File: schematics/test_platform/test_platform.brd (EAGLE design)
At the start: 100 x 65 mm, 13 parts

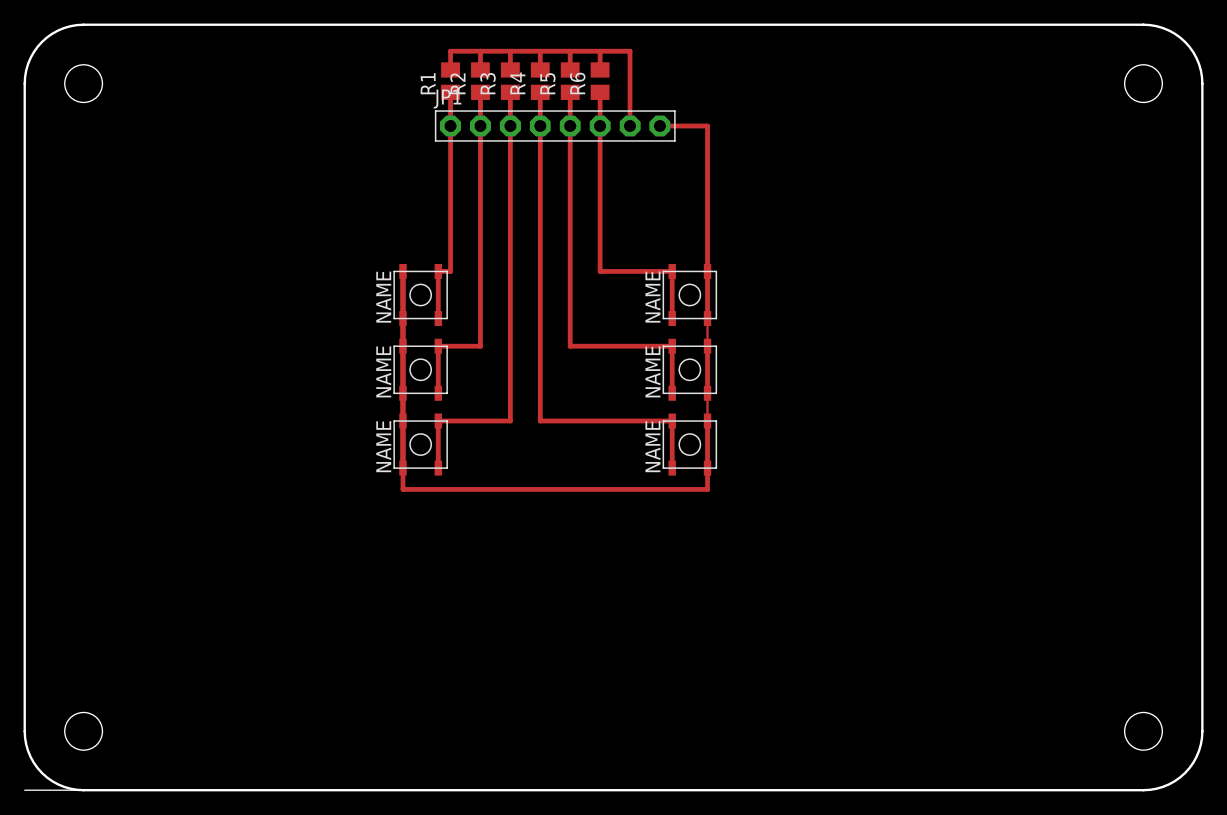
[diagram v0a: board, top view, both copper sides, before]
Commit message: test platform ready for production, except for button footprints
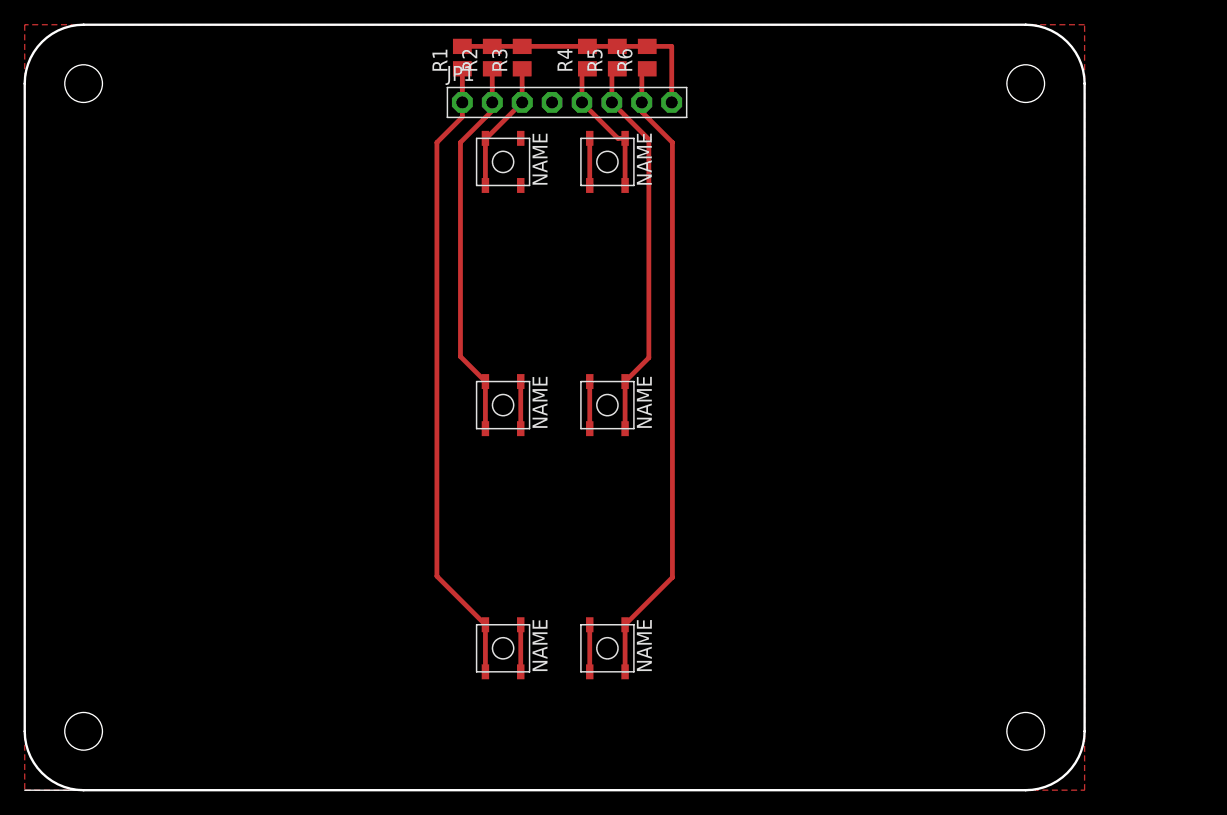
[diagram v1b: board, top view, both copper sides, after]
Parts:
- moved U$1 30.8 mm to (40.6, 12.1), turned to 180 degrees
- moved U$4 30.8 mm to (49.5, 12.1), turned to 180 degrees
- moved U$3 25.0 mm to (40.6, 53.4), turned to 180 degrees
- moved U$6 25.0 mm to (49.5, 53.4), turned to 180 degrees
- moved U$2 7.62 mm to (40.6, 32.7), turned to 180 degrees
- moved U$5 7.62 mm to (49.5, 32.7), turned to 180 degrees
- moved R4 4.47 mm to (47.8, 62.2)
- moved R5 4.47 mm to (50.3, 62.2)
- moved R6 4.47 mm to (52.9, 62.2)
- moved JP1 2.24 mm to (46.0, 58.4)
- moved R1 2.24 mm to (37.2, 62.2)
- moved R2 2.24 mm to (39.7, 62.2)
- moved R3 2.24 mm to (42.2, 62.2)
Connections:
- removed net N$7: JP1.7, R1.2, R2.2, R3.2, R4.2, R5.2, R6.2
- removed net N$8: JP1.8, U$1.A1, U$1.A2, U$2.A1, U$2.A2, U$3.A1, U$3.A2, U$4.B1, U$4.B2, U$5.B1, U$5.B2, U$6.B1, U$6.B2
- new net GND: JP1.4, U$1.A1, U$1.A2, U$2.A1, U$2.A2, U$3.A1, U$3.A2, U$4.B1, U$4.B2, U$5.B1, U$5.B2, U$6.B1, U$6.B2
- new net VCC: JP1.8, R1.2, R2.2, R3.2, R4.2, R5.2, R6.2
- net N$4: now also JP1.5; no longer JP1.4
- net N$5: now also JP1.6; no longer JP1.5
- net N$6: now also JP1.7; no longer JP1.6
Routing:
- net N$8: track 96.0 -> 0.00 mm
- net N$1: track 20.2 -> 53.8 mm
- net N$7: track 31.1 -> 0.00 mm
- net N$4: track 43.1 -> 12.2 mm
- net N$6: track 25.3 -> 54.4 mm
- net N$3: track 38.0 -> 11.2 mm
- net VCC: track 0.00 -> 23.0 mm
- net GND: track 0.00 -> 20.0 mm
- net N$2: track 29.1 -> 32.6 mm
- net N$5: track 34.2 -> 33.2 mm
- added copper zone on layer 1, net GND
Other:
- board size 100 x 65 mm -> 90 x 65 mm

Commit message: circuit for testplatform done
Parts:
- moved U$6 41.4 mm to (50.0, 12.0)
- moved U$4 40.0 mm to (50.0, 52.0), turned to 0 degrees
- moved U$3 1.49 mm to (40.0, 52.0), turned to 0 degrees
- moved U$2 0.94 mm to (40.0, 32.0)
- moved U$5 0.87 mm to (50.0, 32.0)
- moved U$1 0.62 mm to (40.0, 12.0)
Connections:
- net N$4: now also U$4.A1, U$4.A2; no longer U$6.A1, U$6.A2
- net N$6: now also U$6.A1, U$6.A2; no longer U$4.A1, U$4.A2
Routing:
- net GND: track 20.0 -> 0.00 mm
- net N$3: track 11.2 -> 13.3 mm
- net N$1: track 53.8 -> 55.8 mm
- net N$6: track 54.4 -> 56.1 mm
- net N$4: track 12.2 -> 13.8 mm
- net N$5: track 33.2 -> 34.6 mm
- net N$2: track 32.6 -> 34.0 mm
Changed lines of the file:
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@@
 <elements>
 <element name="JP1" library="adafruit" package="1X08-BIG" value="" x="46.05" y="58.4"/>
-<element name="U$1" library="BraillePad" package="SMT-BUTTON" value="SMT_BUTTON" x="40.62" y="12.05" rot="R180"/>
-<element name="U$2" library="BraillePad" package="SMT-BUTTON" value="SMT_BUTTON" x="40.62" y="32.7" rot="R180"/>
-<element name="U$3" library="BraillePad" package="SMT-BUTTON" value="SMT_BUTTON" x="40.62" y="53.35" rot="R180"/>
-<element name="U$4" library="BraillePad" package="SMT-BUTTON" value="SMT_BUTTON" x="49.48" y="12.05" rot="R180"/>
-<element name="U$5" library="BraillePad" package="SMT-BUTTON" value="SMT_BUTTON" x="49.48" y="32.7" rot="R180"/>
-<element name="U$6" library="BraillePad" package="SMT-BUTTON" value="SMT_BUTTON" x="49.48" y="53.35" rot="R180"/>
 <element name="R1" library="rcl" package="M0805" value="" x="37.16" y="62.21" rot="R90"/>
 <element name="R2" library="rcl" package="M0805" value="" x="39.7" y="62.21" rot="R90"/>
@@
 <element name="R6" library="rcl" package="M0805" value="" x="52.86" y="62.21" rot="R90"/>
 <element name="R5" library="rcl" package="M0805" value="" x="50.32" y="62.21" rot="R90"/>
+<element name="U$1" library="BraillePad" package="SMT-BUTTON" value="SMT_BUTTON" x="40" y="12" rot="R180"/>
+<element name="U$2" library="BraillePad" package="SMT-BUTTON" value="SMT_BUTTON" x="40" y="32" rot="R180"/>
+<element name="U$3" library="BraillePad" package="SMT-BUTTON" value="SMT_BUTTON" x="40" y="52"/>
+<element name="U$4" library="BraillePad" package="SMT-BUTTON" value="SMT_BUTTON" x="50" y="52"/>
+<element name="U$5" library="BraillePad" package="SMT-BUTTON" value="SMT_BUTTON" x="50" y="32" rot="R180"/>
+<element name="U$6" library="BraillePad" package="SMT-BUTTON" value="SMT_BUTTON" x="50" y="12" rot="R180"/>
 </elements>
 <signals>
 <signal name="N$1">
 <contactref element="JP1" pad="1"/>
+<contactref element="R1" pad="1"/>
+<wire x1="37.16" y1="58.4" x2="37.16" y2="61.26" width="0.4064" layer="1"/>
 <contactref element="U$1" pad="B1"/>
 <contactref element="U$1" pad="B2"/>
-<contactref element="R1" pad="1"/>
-<wire x1="37.16" y1="58.4" x2="37.16" y2="61.26" width="0.4064" layer="1"/>
-<wire x1="39.12" y1="14.05" x2="39.12" y2="10.05" width="0.4064" layer="1"/>
-<wire x1="37.16" y1="58.4" x2="37.16" y2="57.16" width="0.4064" layer="1"/>
-<wire x1="37.16" y1="57.16" x2="35" y2="55" width="0.4064" layer="1"/>
-<wire x1="35" y1="55" x2="35" y2="18.17" width="0.4064" layer="1"/>
-<wire x1="35" y1="18.17" x2="39.12" y2="14.05" width="0.4064" layer="1"/>
+<wire x1="37.16" y1="58.4" x2="36.4" y2="58.4" width="0.4064" layer="1"/>
+<wire x1="36.4" y1="58.4" x2="35" y2="57" width="0.4064" layer="1"/>
+<wire x1="35" y1="57" x2="35" y2="18.9" width="0.4064" layer="1"/>
+<wire x1="35" y1="18.9" x2="37.9" y2="16" width="0.4064" layer="1"/>
+<wire x1="37.9" y1="16" x2="37.9" y2="8" width="0.4064" layer="1"/>
 </signal>
 <signal name="N$2">
 <contactref element="JP1" pad="2"/>
+<contactref element="R2" pad="1"/>
+<wire x1="39.7" y1="58.4" x2="39.7" y2="61.26" width="0.4064" layer="1"/>
 <contactref element="U$2" pad="B1"/>
 <contactref element="U$2" pad="B2"/>
-<contactref element="R2" pad="1"/>
-<wire x1="39.7" y1="58.4" x2="39.7" y2="61.26" width="0.4064" layer="1"/>
-<wire x1="39.12" y1="34.7" x2="39.12" y2="30.7" width="0.4064" layer="1"/>
-<wire x1="39.7" y1="58.4" x2="39.7" y2="57.7" width="0.4064" layer="1"/>
-<wire x1="39.7" y1="57.7" x2="37" y2="55" width="0.4064" layer="1"/>
-<wire x1="37" y1="55" x2="37" y2="36.82" width="0.4064" layer="1"/>
-<wire x1="37" y1="36.82" x2="39.12" y2="34.7" width="0.4064" layer="1"/>
+<wire x1="39.7" y1="58.4" x2="39.7" y2="37.8" width="0.4064" layer="1"/>
+<wire x1="39.7" y1="37.8" x2="37.9" y2="36" width="0.4064" layer="1"/>
+<wire x1="37.9" y1="28" x2="37.9" y2="36" width="0.4064" layer="1"/>
 </signal>
 <signal name="N$3">
 <contactref element="JP1" pad="3"/>
+<contactref element="R3" pad="1"/>
+<wire x1="42.24" y1="58.4" x2="42.24" y2="61.26" width="0.4064" layer="1"/>
 <contactref element="U$3" pad="B1"/>
 <contactref element="U$3" pad="B2"/>
-<contactref element="R3" pad="1"/>
-<wire x1="42.24" y1="58.4" x2="42.24" y2="61.26" width="0.4064" layer="1"/>
-<wire x1="39.12" y1="55.35" x2="39.12" y2="51.35" width="0.4064" layer="1"/>
-<wire x1="42.24" y1="58.4" x2="39.19" y2="55.35" width="0.4064" layer="1"/>
-<wire x1="39.19" y1="55.35" x2="39.12" y2="55.35" width="0.4064" layer="1"/>
+<wire x1="42.24" y1="58.4" x2="42.1" y2="56" width="0.4064" layer="1"/>
+<wire x1="42.1" y1="48" x2="42.1" y2="56" width="0.4064" layer="1"/>
 </signal>
 <signal name="N$4">
-<contactref element="U$6" pad="A1"/>
-<contactref element="U$6" pad="A2"/>
 <contactref element="R4" pad="1"/>
-<wire x1="50.98" y1="55.35" x2="50.98" y2="51.35" width="0.4064" layer="1"/>
 <contactref element="JP1" pad="5"/>
 <wire x1="47.78" y1="61.26" x2="47.32" y2="61.26" width="0.4064" layer="1"/>
 <wire x1="47.32" y1="61.26" x2="47.32" y2="58.4" width="0.4064" layer="1"/>
-<wire x1="47.32" y1="58.4" x2="50.37" y2="55.35" width="0.4064" layer="1"/>
-<wire x1="50.37" y1="55.35" x2="50.98" y2="55.35" width="0.4064" layer="1"/>
+<contactref element="U$4" pad="A2"/>
+<contactref element="U$4" pad="A1"/>
+<wire x1="47.32" y1="58.4" x2="47.9" y2="56" width="0.4064" layer="1"/>
+<wire x1="47.9" y1="48" x2="47.9" y2="56" width="0.4064" layer="1"/>
 </signal>
 <signal name="N$5">
-<contactref element="U$5" pad="A1"/>
-<contactref element="U$5" pad="A2"/>
 <contactref element="R5" pad="1"/>
-<wire x1="50.98" y1="30.7" x2="50.98" y2="34.7" width="0.4064" layer="1"/>
 <contactref element="JP1" pad="6"/>
 <wire x1="50.32" y1="61.26" x2="49.86" y2="61.26" width="0.4064" layer="1"/>
 <wire x1="49.86" y1="61.26" x2="49.86" y2="58.4" width="0.4064" layer="1"/>
-<wire x1="49.86" y1="58.4" x2="53" y2="55.26" width="0.4064" layer="1"/>
-<wire x1="53" y1="55.26" x2="53" y2="36.72" width="0.4064" layer="1"/>
-<wire x1="53" y1="36.72" x2="50.98" y2="34.7" width="0.4064" layer="1"/>
+<contactref element="U$5" pad="A2"/>
+<contactref element="U$5" pad="A1"/>
+<wire x1="49.86" y1="58.4" x2="49.86" y2="38.24" width="0.4064" layer="1"/>
+<wire x1="49.86" y1="38.24" x2="52.1" y2="36" width="0.4064" layer="1"/>
+<wire x1="52.1" y1="28" x2="52.1" y2="36" width="0.4064" layer="1"/>
 </signal>
 <signal name="N$6">
-<contactref element="U$4" pad="A1"/>
-<contactref element="U$4" pad="A2"/>
 <contactref element="R6" pad="1"/>
-<wire x1="50.98" y1="10.05" x2="50.98" y2="14.05" width="0.4064" layer="1"/>
 <contactref element="JP1" pad="7"/>
 <wire x1="52.86" y1="61.26" x2="52.4" y2="61.26" width="0.4064" layer="1"/>
 <wire x1="52.4" y1="61.26" x2="52.4" y2="58.4" width="0.4064" layer="1"/>
-<wire x1="52.4" y1="58.4" x2="52.4" y2="57.6" width="0.4064" layer="1"/>
-<wire x1="52.4" y1="57.6" x2="55" y2="55" width="0.4064" layer="1"/>
-<wire x1="55" y1="55" x2="55" y2="18.07" width="0.4064" layer="1"/>
-<wire x1="55" y1="18.07" x2="50.98" y2="14.05" width="0.4064" layer="1"/>
+<contactref element="U$6" pad="A2"/>
+<contactref element="U$6" pad="A1"/>
+<wire x1="52.4" y1="58.4" x2="52.6" y2="58.4" width="0.4064" layer="1"/>
+<wire x1="52.6" y1="58.4" x2="55" y2="56" width="0.4064" layer="1"/>
+<wire x1="55" y1="56" x2="55" y2="18.9" width="0.4064" layer="1"/>
+<wire x1="55" y1="18.9" x2="52.1" y2="16" width="0.4064" layer="1"/>
+<wire x1="52.1" y1="8" x2="52.1" y2="16" width="0.4064" layer="1"/>
 </signal>
 <signal name="GND">
-<contactref element="U$6" pad="B1"/>
-<contactref element="U$6" pad="B2"/>
-<contactref element="U$5" pad="B1"/>
-<contactref element="U$5" pad="B2"/>
-<contactref element="U$4" pad="B1"/>
-<contactref element="U$4" pad="B2"/>
-<contactref element="U$3" pad="A1"/>
-<contactref element="U$3" pad="A2"/>
-<contactref element="U$1" pad="A1"/>
-<contactref element="U$1" pad="A2"/>
-<contactref element="U$2" pad="A1"/>
-<contactref element="U$2" pad="A2"/>
-<wire x1="42.12" y1="10.05" x2="42.12" y2="14.05" width="0.4064" layer="1"/>
-<wire x1="42.12" y1="30.7" x2="42.12" y2="34.7" width="0.4064" layer="1"/>
-<wire x1="47.98" y1="51.35" x2="47.98" y2="55.35" width="0.4064" layer="1"/>
-<wire x1="47.98" y1="30.7" x2="47.98" y2="34.7" width="0.4064" layer="1"/>
-<wire x1="47.98" y1="14.05" x2="47.98" y2="10.05" width="0.4064" layer="1"/>
 <contactref element="JP1" pad="4"/>
 <polygon width="0.4064" layer="1">
@@
 <vertex x="90" y="65"/>
 </polygon>
+<contactref element="U$1" pad="A2"/>
+<contactref element="U$1" pad="A1"/>
+<contactref element="U$2" pad="A2"/>
+<contactref element="U$2" pad="A1"/>
+<contactref element="U$3" pad="A2"/>
+<contactref element="U$3" pad="A1"/>
+<contactref element="U$4" pad="B1"/>
+<contactref element="U$4" pad="B2"/>
+<contactref element="U$5" pad="B1"/>
+<contactref element="U$5" pad="B2"/>
+<contactref element="U$6" pad="B1"/>
+<contactref element="U$6" pad="B2"/>
 </signal>
 <signal name="VCC">
